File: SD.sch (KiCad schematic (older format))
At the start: 9 parts, among them J402 Micro_SD_Card

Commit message: libs added
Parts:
- D401, D402: symbol ESP-Audio-rescue:SP0503BAHT-Power_Protection -> ESP32-Eurorack-Audio-rescue:SP0503BAHT-Power_Protection-ESP-Audio-rescue
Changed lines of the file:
@@
 EESchema Schematic File Version 4
+LIBS:ESP32-Eurorack-Audio-cache
 EELAYER 29 0
 EELAYER END
@@
 	6700 1950 6700 2000
 $Comp
-L ESP-Audio-rescue:SP0503BAHT-Power_Protection D401
+L ESP32-Eurorack-Audio-rescue:SP0503BAHT-Power_Protection-ESP-Audio-rescue D401
 U 1 1 5B682E0A
 P 5550 3300
@@
 $EndComp
 $Comp
-L ESP-Audio-rescue:SP0503BAHT-Power_Protection D402
+L ESP32-Eurorack-Audio-rescue:SP0503BAHT-Power_Protection-ESP-Audio-rescue D402
 U 1 1 5B682E68
 P 6500 3300

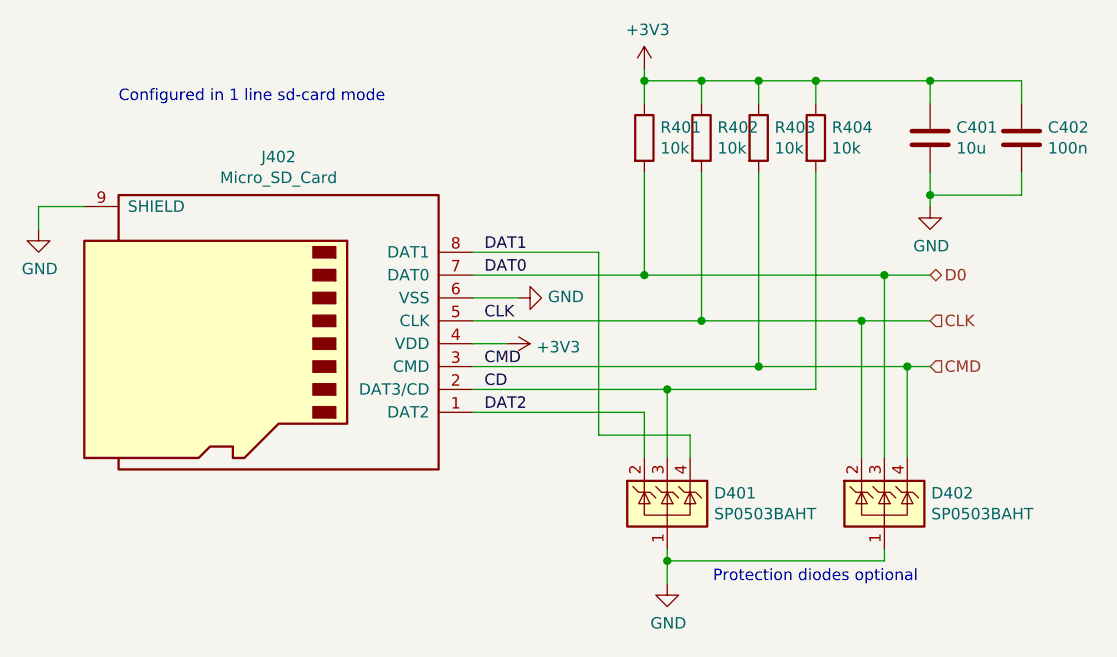
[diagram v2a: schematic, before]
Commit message: cleaned up schematic
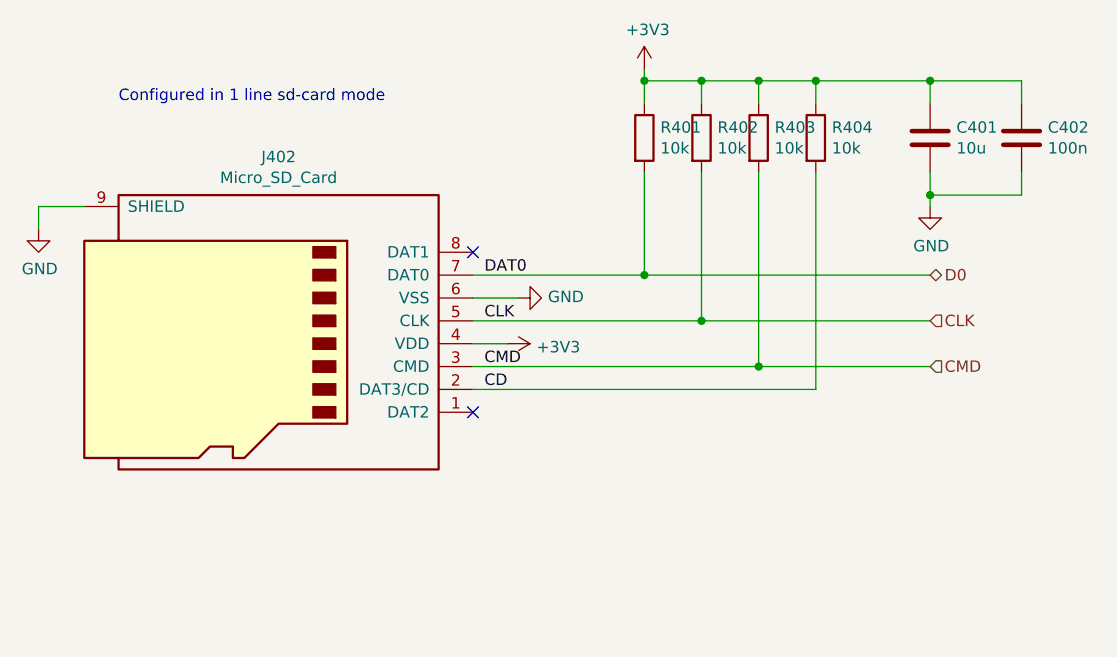
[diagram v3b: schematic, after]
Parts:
- removed D401, D402: SP0503BAHT, Package_TO_SOT_SMD:SOT-143, symbol ESP32-Eurorack-Audio-rescue:SP0503BAHT-Power_Protection-ESP-Audio-rescue
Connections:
- net DAT1: no longer names the net of J402.8 (DAT1)
- net DAT2: no longer names the net of J402.1 (DAT2)
- no-connect marks 0 -> 2
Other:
- note removed: "Protection diodes optional"
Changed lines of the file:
@@
 Sheet 4 8
 Title "ESP32 Eurorack Audio Module"
-Date "2019-03-27"
-Rev "C"
+Date "2019-05-13"
+Rev "D"
 Comp "(c) Robert Manzke 2019"
 Comment1 "https://creativecommons.org/licenses/by-nc-sa/4.0/"
@@
 	5950 2700 5950 1850
 Wire Wire Line
-	4700 2800 5550 2800
-Wire Wire Line
 	6200 2800 6200 1850
 $Comp
@@
 Wire Wire Line
 	5950 1450 5700 1450
-Wire Wire Line
-	5450 2300 6500 2300
 Connection ~ 5450 2300
-Wire Wire Line
-	5700 2500 6400 2500
 Connection ~ 5700 2500
-Wire Wire Line
-	5950 2700 6600 2700
 Connection ~ 5950 2700
 Text HLabel 6700 2300 2    50   BiDi ~ 0
@@
 Wire Wire Line
 	6700 1950 6700 2000
-$Comp
-L ESP32-Eurorack-Audio-rescue:SP0503BAHT-Power_Protection-ESP-Audio-rescue D401
-U 1 1 5B682E0A
-P 5550 3300
-AR Path="/5B682E0A" Ref="D401"  Part="1"
-AR Path="/5B67C7FC/5B682E0A" Ref="D401"  Part="1"
-F 0 "D401" H 5755 3346 50  0000 L CNN
-F 1 "SP0503BAHT" H 5755 3255 50  0000 L CNN
-F 2 "Package_TO_SOT_SMD:SOT-143" H 5775 3250 50  0001 L CNN
-F 3 "http://www.littelfuse.com/~/media/files/littelfuse/technical%20resources/documents/data%20sheets/sp05xxba.pdf" H 5675 3425 50  0001 C CNN
-	1    5550 3300
-	1    0    0    -1
-$EndComp
-$Comp
-L ESP32-Eurorack-Audio-rescue:SP0503BAHT-Power_Protection-ESP-Audio-rescue D402
-U 1 1 5B682E68
-P 6500 3300
-AR Path="/5B682E68" Ref="D402"  Part="1"
-AR Path="/5B67C7FC/5B682E68" Ref="D402"  Part="1"
-F 0 "D402" H 6705 3346 50  0000 L CNN
-F 1 "SP0503BAHT" H 6705 3255 50  0000 L CNN
-F 2 "Package_TO_SOT_SMD:SOT-143" H 6725 3250 50  0001 L CNN
-F 3 "http://www.littelfuse.com/~/media/files/littelfuse/technical%20resources/documents/data%20sheets/sp05xxba.pdf" H 6625 3425 50  0001 C CNN
-	1    6500 3300
-	1    0    0    -1
-$EndComp
-$Comp
-L power:GND #PWR0408
-U 1 1 5B682EC3
-P 5550 3650
-F 0 "#PWR0408" H 5550 3400 50  0001 C CNN
-F 1 "GND" H 5555 3477 50  0000 C CNN
-F 2 "" H 5550 3650 50  0001 C CNN
-F 3 "" H 5550 3650 50  0001 C CNN
-	1    5550 3650
-	1    0    0    -1
-$EndComp
-Wire Wire Line
-	5550 3500 5550 3550
-Wire Wire Line
-	6500 3500 6500 3550
-Wire Wire Line
-	6500 3550 5550 3550
-Connection ~ 5550 3550
-Wire Wire Line
-	5550 3550 5550 3650
-Wire Wire Line
-	4700 2900 5450 2900
-Wire Wire Line
-	5450 2900 5450 3100
-Wire Wire Line
-	5550 3100 5550 2800
-Connection ~ 5550 2800
-Wire Wire Line
-	5550 2800 6200 2800
-Wire Wire Line
-	6400 3100 6400 2500
-Connection ~ 6400 2500
-Wire Wire Line
-	6400 2500 6700 2500
-Wire Wire Line
-	6500 3100 6500 2300
-Connection ~ 6500 2300
-Wire Wire Line
-	6500 2300 6700 2300
-Wire Wire Line
-	5250 3000 5250 2200
-Wire Wire Line
-	5250 2200 4700 2200
 $Comp
 L Connector:Micro_SD_Card J402
@@
 	-1   0    0    1
 $EndComp
-Text Label 4750 2200 0    50   ~ 0
-DAT1
 Text Label 4750 2300 0    50   ~ 0
 DAT0
@@
 Text Label 4750 2800 0    50   ~ 0
 CD
-Text Label 4750 2900 0    50   ~ 0
-DAT2
 Wire Wire Line
 	4700 2700 5950 2700
-Wire Wire Line
-	5250 3000 5650 3000
-Wire Wire Line
-	5650 3000 5650 3100
-Wire Wire Line
-	6600 3100 6600 2700
-Connection ~ 6600 2700
-Wire Wire Line
-	6600 2700 6700 2700
 Text Notes 3150 1550 0    50   ~ 0
 Configured in 1 line sd-card mode
-Text Notes 5750 3650 0    50   ~ 0
-Protection diodes optional
+Wire Wire Line
+	4700 2800 6200 2800
+Wire Wire Line
+	5950 2700 6700 2700
+Wire Wire Line
+	5450 2300 6700 2300
+Wire Wire Line
+	5700 2500 6700 2500
+NoConn ~ 4700 2200
+NoConn ~ 4700 2900
 $EndSCHEMATC
